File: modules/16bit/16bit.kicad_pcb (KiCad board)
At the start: 2 copper layers, 30.5 x 68.6 mm, 55 parts, among them J1 Conn_01x08_Socket, J2 Conn_01x08_Socket, J5 USB_C_Receptacle_USB2.0_14P, SW1 K2-1808SN-A4SW-01, SW2 K2-1808SN-A4SW-01, SW3 K2-1808SN-A4SW-01, U1 RP2350_60QFN, U2 W25Q128JVS, U3 MCP6002-xSN, U4 PT8211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

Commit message: set 1k for the DAC low pass filter
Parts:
- R17, R18: value 10k -> 1k
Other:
- board text added: "16BIT 0.2.0"
- board text removed: "16BIT 0.1.0"
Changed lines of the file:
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@@
 			)
 		)
-		(property "Value" "10k"
+		(property "Value" "1k"
 			(at 0 1.17 0)
 			(layer "F.Fab")
@@
 			)
 		)
-		(property "Value" "10k"
+		(property "Value" "1k"
 			(at 0 1.17 0)
 			(layer "F.Fab")
@@
 		)
 	)
-	(gr_text "16BIT\n0.1.0"
+	(gr_text "16BIT\n0.2.0"
 		(at 76.327 107.95 0)
 		(layer "F.SilkS")

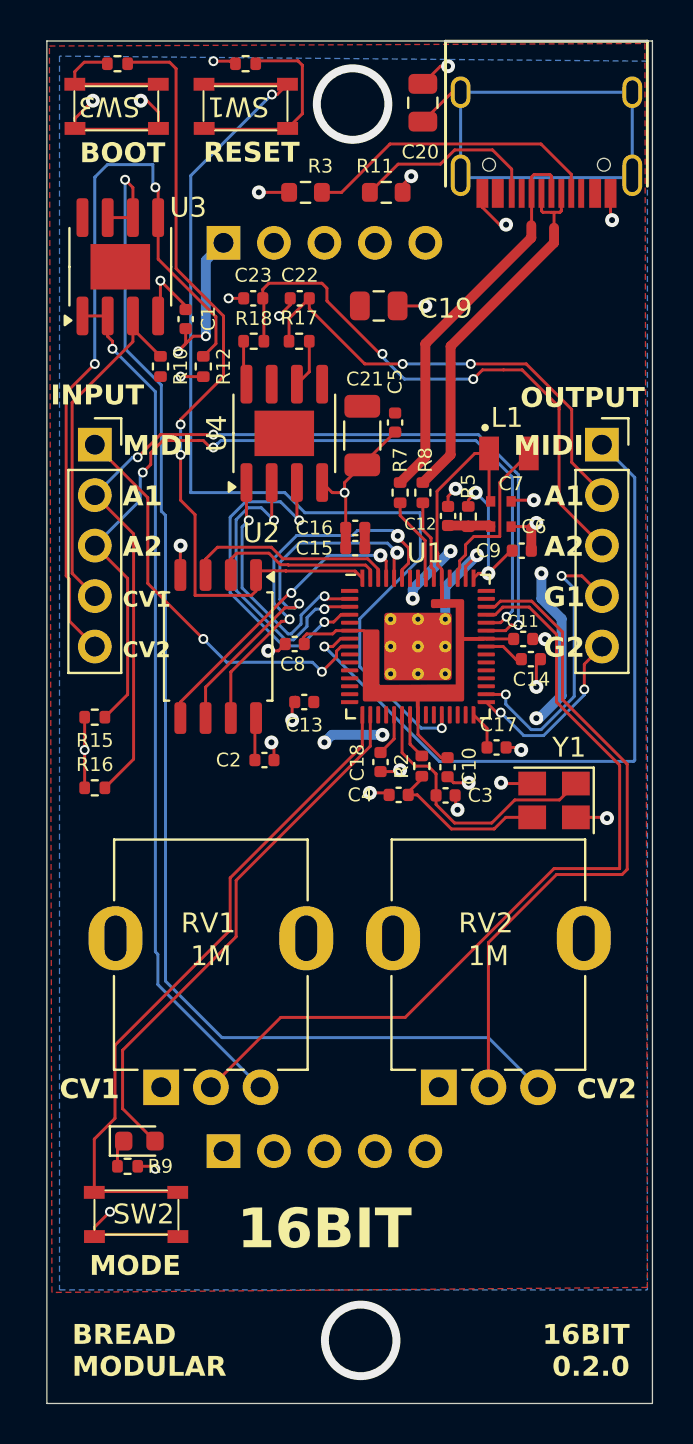
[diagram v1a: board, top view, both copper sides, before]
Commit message: Add 4677 PSRAM
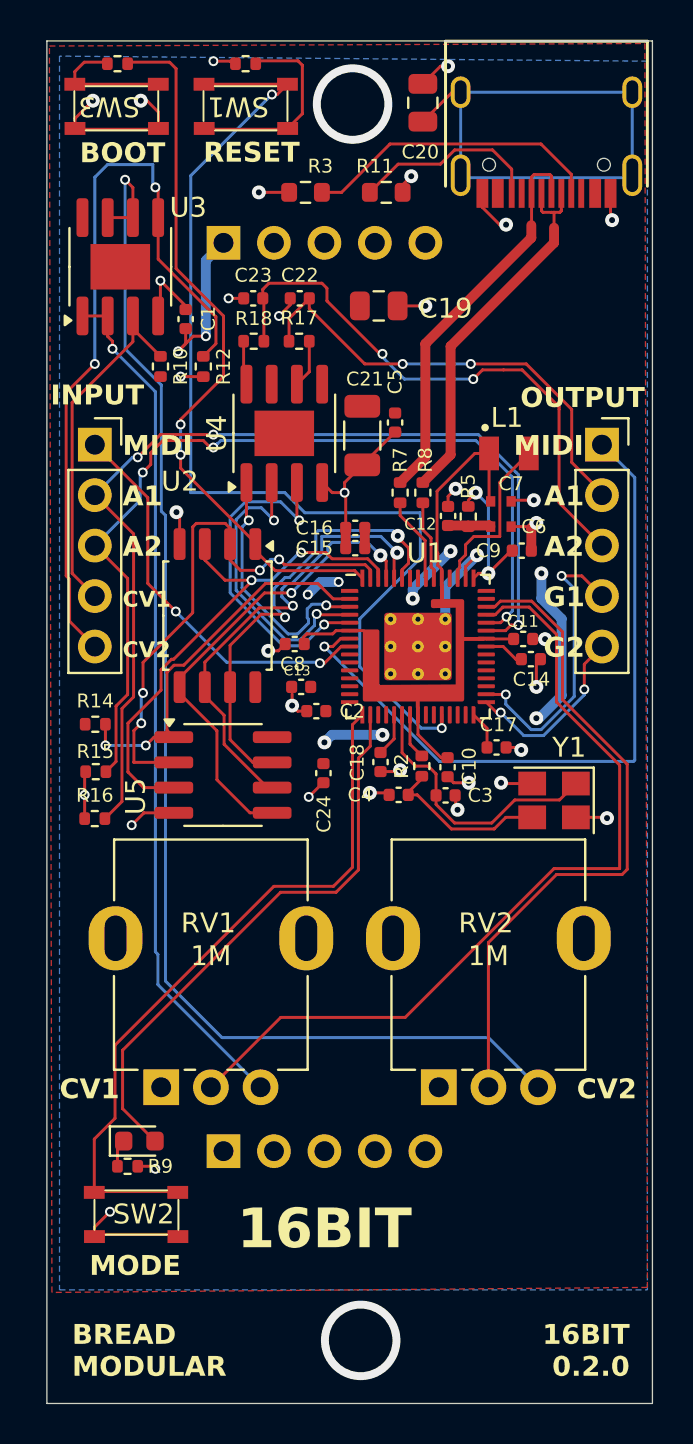
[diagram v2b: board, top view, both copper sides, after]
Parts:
- added C24: 100n, Capacitor_SMD:C_0402_1005Metric, F.Cu at (60.9, 77.5)
- added R14: 10k, Resistor_SMD:R_0402_1005Metric, F.Cu at (49.4, 75.0)
- added U5: 4677, BreadModular_MISC:SOIC-8 Generic, F.Cu at (55.8, 77.8)
- moved C2 3.59 mm to (60.6, 74.4), turned to 180 degrees
- moved R15 2.74 mm to (49.5, 77.4)
- moved U2 1.56 mm to (55.6, 69.6)
- moved R16 1.55 mm to (49.4, 79.8)
- moved C13 0.78 mm to (59.8, 73.2)
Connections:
- U1 pad 2: BCK -> PSRAM_CS
- U1 pad 3: WS -> BCK
- U1 pad 4: DIN -> WS
- U1 pad 5: unconnected-(U1-GPIO3-Pad5) -> DIN
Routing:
- net PSRAM_CS: track 0.00 -> 19.5 mm, vias 0 -> 2
- net /QSPI_SD1: track 8.72 -> 26.9 mm, vias 0 -> 4
- net /QSPI_SD2: track 10.6 -> 26.3 mm, vias 0 -> 2
- net /QSPI_SD0: track 15.2 -> 23.6 mm
- net /QSPI_SCLK: track 19.0 -> 23.7 mm
- net QSPI_SS: track 40.8 -> 36.2 mm
- net /QSPI_SD3: track 19.3 -> 23.2 mm
- net AIN_2: track 43.4 -> 46.2 mm
- net /GPIO12: track 33.8 -> 35.5 mm
- net GND: track 81.4 -> 83.1 mm, vias 33 -> 34
- net /GPIO13: track 27.3 -> 28.9 mm
- net AIN_1: track 48.9 -> 50.4 mm
- net MIDI_IN: track 20.8 -> 20.3 mm
- net +3V3: track 35.7 -> 35.3 mm, vias 9 -> 11

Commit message: Make sure the PSRAM is hand solderable
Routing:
- net /QSPI_SCLK: track 23.7 -> 24.4 mm
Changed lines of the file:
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@@
 		(at 55.8496 77.8358)
 		(property "Reference" "U5"
-			(at -4.3892 0.828 90)
+			(at -4.4654 1.1836 90)
 			(unlocked yes)
 			(layer "F.SilkS")
 			(effects
 				(font
-					(size 1 1)
-					(thickness 0.1)
+					(size 0.8 0.8)
+					(thickness 0.2)
+					(bold yes)
 				)
 			)
@@
 		(pad "1" smd roundrect
 			(at -2.47 -2.155)
-			(size 1.95 0.6)
+			(size 2.6 0.8)
 			(layers "F.Cu" "F.Paste" "F.Mask")
 			(roundrect_rratio 0.25)
@@
 		(pad "2" smd roundrect
 			(at -2.47 -0.885)
-			(size 1.95 0.6)
+			(size 2.6 0.8)
 			(layers "F.Cu" "F.Paste" "F.Mask")
 			(roundrect_rratio 0.25)
@@
 		(pad "3" smd roundrect
 			(at -2.47 0.385)
-			(size 1.95 0.6)
+			(size 2.6 0.8)
 			(layers "F.Cu" "F.Paste" "F.Mask")
 			(roundrect_rratio 0.25)
@@
 		(pad "4" smd roundrect
 			(at -2.47 1.655)
-			(size 1.95 0.6)
+			(size 2.6 0.8)
 			(layers "F.Cu" "F.Paste" "F.Mask")
 			(roundrect_rratio 0.25)
@@
 		(pad "5" smd roundrect
 			(at 2.48 1.655)
-			(size 1.95 0.6)
+			(size 2.6 0.8)
 			(layers "F.Cu" "F.Paste" "F.Mask")
 			(roundrect_rratio 0.25)
@@
 		(pad "6" smd roundrect
 			(at 2.48 0.385)
-			(size 1.95 0.6)
+			(size 2.6 0.8)
 			(layers "F.Cu" "F.Paste" "F.Mask")
 			(roundrect_rratio 0.25)
@@
 		(pad "7" smd roundrect
 			(at 2.48 -0.885)
-			(size 1.95 0.6)
+			(size 2.6 0.8)
 			(layers "F.Cu" "F.Paste" "F.Mask")
 			(roundrect_rratio 0.25)
@@
 		(pad "8" smd roundrect
 			(at 2.48 -2.155)
-			(size 1.95 0.6)
+			(size 2.6 0.8)
 			(layers "F.Cu" "F.Paste" "F.Mask")
 			(roundrect_rratio 0.25)
@@
 		(tags "capacitor")
 		(property "Reference" "C8"
-			(at 0.099 -1.016 0)
+			(at -0.0736 0.9398 0)
 			(layer "F.SilkS")
 			(effects
@@
 		(tags "capacitor")
 		(property "Reference" "C2"
-			(at -1.806 0 0)
+			(at -0.0534 -0.9144 0)
 			(layer "F.SilkS")
 			(effects
@@
 	)
 	(segment
-		(start 57.354601 76.9508)
-		(end 56.2102 75.806399)
+		(start 64.652075 65.821423)
+		(end 64.857991 65.821423)
 		(width 0.15)
 		(layer "F.Cu")
@@
 	)
 	(segment
-		(start 64.652075 65.821423)
-		(end 64.857991 65.821423)
+		(start 58.3296 76.9508)
+		(end 56.8594 76.9508)
+		(width 0.15)
+		(layer "F.Cu")
+		(net 46)
+	)
+	(segment
+		(start 56.2102 76.3016)
+		(end 56.2102 73.1638)
 		(width 0.15)
 		(layer "F.Cu")
@@
 	)
 	(segment
-		(start 56.2102 75.806399)
-		(end 56.2102 73.1638)
-		(width 0.15)
-		(layer "F.Cu")
-		(net 46)
-	)
-	(segment
-		(start 58.3296 76.9508)
-		(end 57.354601 76.9508)
-		(width 0.15)
-		(layer "F.Cu")
-		(net 46)
-	)
-	(segment
 		(start 65.194818 66.15825)
 		(end 65.194818 66.927388)
@@
 	)
 	(segment
+		(start 56.8594 76.9508)
+		(end 56.2102 76.3016)
+		(width 0.15)
+		(layer "F.Cu")
+		(net 46)
+	)
+	(segment
 		(start 56.2102 71.061664)
 		(end 56.2102 73.1638)
@@
 	)
 	(segment
-		(start 54.9402 73.6092)
-		(end 54.9402 73.1638)
+		(start 55.9102 74.5792)
+		(end 54.9402 73.6092)
 		(width 0.15)
 		(layer "F.Cu")
@@
 	)
 	(segment
-		(start 55.9102 74.5792)
-		(end 54.9402 73.6092)
+		(start 54.9402 73.6092)
+		(end 54.9402 73.1638)
 		(width 0.15)
 		(layer "F.Cu")
@@
 	)
 	(segment
-		(start 64.619818 66.396423)
-		(end 64.4675 66.548741)
+		(start 58.3296 78.2208)
+		(end 56.8086 78.2208)
 		(width 0.15)
 		(layer "F.Cu")
@@
 	)
 	(segment
-		(start 59.268244 69.173587)
-		(end 57.674013 69.173587)
+		(start 64.619818 66.396423)
+		(end 64.4675 66.548741)
 		(width 0.15)
 		(layer "F.Cu")
@@
 	)
 	(segment
-		(start 54.9402 71.9074)
-		(end 54.9402 73.1638)
+		(start 59.268244 69.173587)
+		(end 57.674013 69.173587)
 		(width 0.15)
 		(layer "F.Cu")
@@
 	)
 	(segment
-		(start 58.090114 78.2208)
-		(end 55.9102 76.040886)
+		(start 56.8086 78.2208)
+		(end 55.9102 77.3224)
 		(width 0.15)
 		(layer "F.Cu")
@@
 	)
 	(segment
-		(start 58.3296 78.2208)
-		(end 58.090114 78.2208)
+		(start 54.9402 71.9074)
+		(end 54.9402 73.1638)
 		(width 0.15)
 		(layer "F.Cu")
@@
 	)
 	(segment
-		(start 55.9102 76.040886)
+		(start 55.9102 77.3224)
 		(end 55.9102 74.5792)
 		(width 0.15)
@@
 	)
 	(segment
-		(start 52.386 75.6808)
-		(end 51.9684 76.0984)
+		(start 51.8448 75.7936)
+		(end 51.9576 75.6808)
 		(width 0.15)
 		(layer "F.Cu")
@@
 	)
 	(segment
-		(start 53.3908 72.0598)
-		(end 53.0352 72.4154)
+		(start 51.9576 75.6808)
+		(end 53.3796 75.6808)
 		(width 0.15)
 		(layer "F.Cu")
@@
 	)
 	(segment
-		(start 53.0352 72.4154)
-		(end 53.0352 75.3364)
+		(start 53.3908 72.0598)
+		(end 53.0352 72.4154)
 		(width 0.15)
 		(layer "F.Cu")
@@
 	)
 	(segment
-		(start 53.3796 75.6808)
-		(end 52.386 75.6808)
+		(start 53.0352 72.4154)
+		(end 53.0352 75.3364)
 		(width 0.15)
 		(layer "F.Cu")
@@
 	)
 	(via
-		(at 51.9684 76.0984)
+		(at 51.8448 75.7936)
 		(size 0.5)
 		(drill 0.3)
@@
 	)
 	(segment
-		(start 51.9684 76.0984)
+		(start 51.8448 75.7936)
+		(end 51.54 76.0984)
+		(width 0.15)
+		(layer "B.Cu")
+		(net 59)
+	)
+	(segment
+		(start 51.54 76.0984)
 		(end 49.9364 76.0984)
 		(width 0.15)

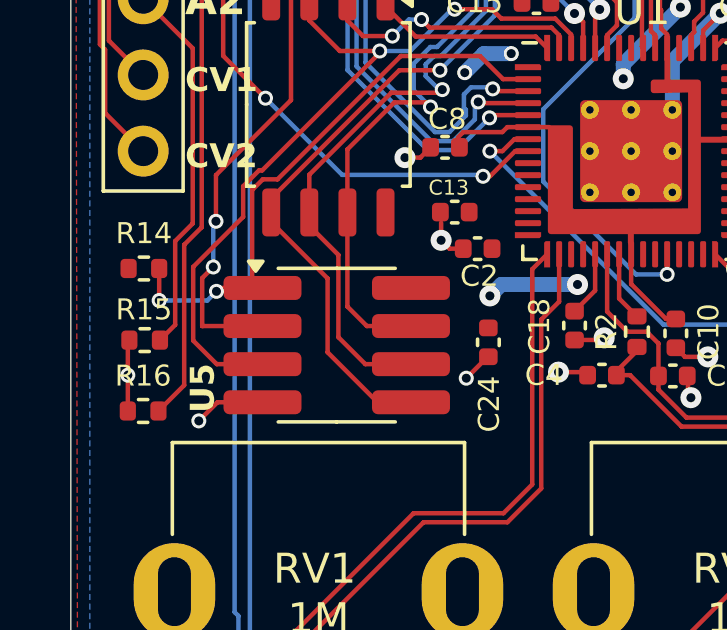
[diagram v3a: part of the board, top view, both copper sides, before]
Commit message: 16bit: update PSRAM support
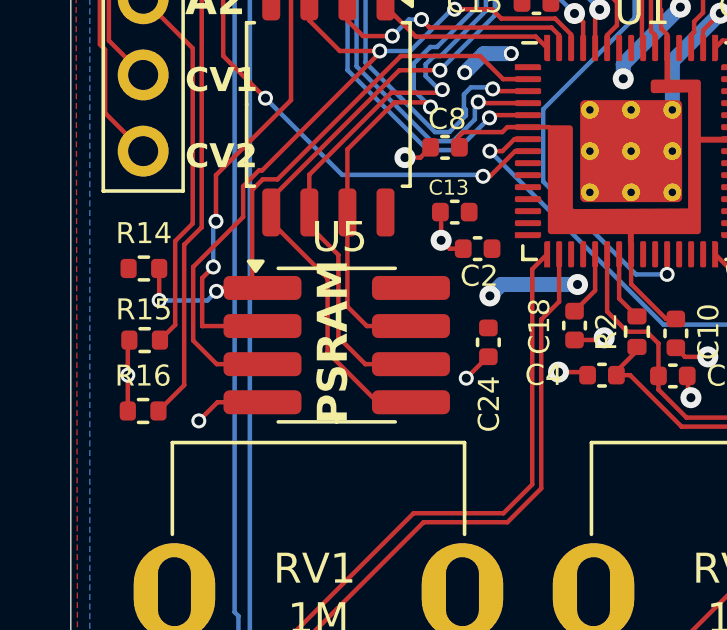
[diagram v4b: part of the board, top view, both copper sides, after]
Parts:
- U5: value 4677 -> PSRAM
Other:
- board text added: "PSRAM"
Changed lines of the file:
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@@
 		(at 55.8496 77.8358)
 		(property "Reference" "U5"
-			(at -4.4654 1.1836 90)
+			(at 0.1 -3.85 0)
 			(unlocked yes)
 			(layer "F.SilkS")
 			(effects
 				(font
-					(size 0.8 0.8)
-					(thickness 0.2)
-					(bold yes)
+					(size 1 1)
+					(thickness 0.1)
 				)
 			)
 		)
-		(property "Value" "4677"
+		(property "Value" "PSRAM"
 			(at 0.25 3.7 0)
 			(unlocked yes)
@@
 		(layer "Edge.Cuts")
 	)
+	(gr_text "PSRAM"
+		(at 56.3118 80.2132 90)
+		(layer "F.SilkS")
+		(effects
+			(font
+				(size 1 1)
+				(thickness 0.2)
+				(bold yes)
+			)
+			(justify left bottom)
+		)
+	)
 	(gr_text "BOOT"

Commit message: 16bit: Add Ditial Audio In & Out support As of now this is currently hardware only. But this allows us to send audio out and in between 16bits digital using a single pin
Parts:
- moved L1 1.48 mm to (68.5, 61.3)
- moved C14 0.53 mm to (70.8, 71.9)
- moved C11 0.13 mm to (70.8, 70.7)
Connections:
- net GOUT_2 renamed DGITIAL_AUDIO_OUT
- J1 pad 5: CV2 -> DGITIAL_AUDIO_IN
- R12 pad 2: CV2 -> Net-(U3B-+)
- U1 pad 12: unconnected-(U1-GPIO8-Pad12) -> DGITIAL_AUDIO_IN
- U3 pad 5: CV2 -> Net-(U3B-+)
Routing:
- net CV2: track 39.2 -> 0.00 mm, vias 2 -> 0
- net DGITIAL_AUDIO_IN: track 0.00 -> 28.2 mm, vias 0 -> 2
- net Net-(U3B-+): track 0.00 -> 8.45 mm
- net +3V3: track 35.3 -> 37.0 mm
- net /VREG_LX: track 8.53 -> 7.47 mm
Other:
- board text added: "16BIT 0.3.0"
- board text added: "DA"
- board text removed: "16BIT 0.2.0"
- board text removed: "G2"

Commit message: Revert "16bit: Add Ditial Audio In & Out support"
This reverts commit 124be004a509aaac87467e57efb917f1b3001793.
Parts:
- moved L1 1.48 mm to (69.9, 61.4)
- moved C14 0.53 mm to (71.4, 71.8)
- moved C11 0.13 mm to (71.0, 70.7)
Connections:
- net DGITIAL_AUDIO_OUT renamed GOUT_2
- J1 pad 5: DGITIAL_AUDIO_IN -> CV2
- R12 pad 2: Net-(U3B-+) -> CV2
- U1 pad 12: DGITIAL_AUDIO_IN -> unconnected-(U1-GPIO8-Pad12)
- U3 pad 5: Net-(U3B-+) -> CV2
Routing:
- net CV2: track 0.00 -> 39.2 mm, vias 0 -> 2
- net DGITIAL_AUDIO_IN: track 28.2 -> 0.00 mm, vias 2 -> 0
- net Net-(U3B-+): track 8.45 -> 0.00 mm
- net +3V3: track 37.0 -> 35.3 mm
- net /VREG_LX: track 7.47 -> 8.53 mm
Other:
- board text added: "16BIT 0.2.0"
- board text added: "G2"
- board text removed: "16BIT 0.3.0"
- board text removed: "DA"

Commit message: 16bit: add more room for captions
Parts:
- J1, J2: moved to B.Cu
- moved L1 2.23 mm to (69.2, 59.3)
- moved C14 1.27 mm to (71.4, 73.0)
- moved C11 1.14 mm to (71.0, 71.9)
- turned J1 to 180 degrees
- turned J2 to 180 degrees
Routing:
- net +1V1: track 17.8 -> 21.8 mm
- net +3V3: track 35.3 -> 37.3 mm, vias 11 -> 12
- net /VREG_LX: track 8.53 -> 10.0 mm
- net GND: track 83.1 -> 83.6 mm, vias 34 -> 33
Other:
- board text added: "16BIT 1.0.0"
- board text removed: "16BIT 0.2.0"
